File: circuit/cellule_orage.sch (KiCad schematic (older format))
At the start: 61 parts, among them Q1 BSS138, Q2 BSS138, Q3 BSS138, U2 TLC274, U4 LM555N, U5 TLP291

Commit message: V0.0 - Ready to route!
V0.0 - First release to routing, next step -> define all footprints
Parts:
- removed R4: 1M, symbol POT-RESCUE-cellule_orage
- removed R9: 50k, symbol POT-RESCUE-cellule_orage
- added D4: LBI_RED 2[mA], symbol Led_Small
- added Q4: MMBF170, SOT-23, symbol MMBF170
- added Q5: BSS138, SOT-23, symbol BSS138
- added R21: 114k, symbol R_Small
- added R22: 100k, symbol R_Small
- added R23: 140k, symbol R_Small
- added R26: 174, symbol R_Small
- added R4: 1M, symbol POT
- added R9: 50k, symbol POT
- added SW1: SPST, symbol SPST
- added U3: LM2903small, symbol LM2903small
- gave numbers to parts that had none: 24
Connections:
- net labels added: amplificator, captors, comparator, high-pass_filter, low-pass_filter, user_threshold
- net labels removed: Timer_out
- wire segments 179 -> 233
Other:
- note added: "Battery protection"
- note added: "Low battery display"
- note added: "User ON/OFF"
- note removed: "Circuit enable"
- moved on the sheet: C10, C12, C6, C7, C8, D1, L1, P5, P6, R14, R15, R24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

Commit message: Some schematic cleanup
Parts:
- C1, C10, C11, C12, C13, C2, C3, C4, C5, C7, C9: footprint (none) -> Capacitors_Tantalum_SMD:TantalC_SizeA_EIA-3216_Reflow
- C6, C8: footprint (none) -> Capacitors_SMD:c_elec_6.3x7.7
- D1: footprint (none) -> Diodes_ThroughHole:Diode_DO-41_SOD81_Horizontal_RM10
- D2, D3, D4: footprint (none) -> LEDs:LED-5MM
- L1: footprint (none) -> Choke_SMD:Choke_SMD_Wuerth-WE-PD2-Typ-L
- P1: footprint (none) -> Connect:USB_Micro-B
- P10, P7, P8: footprint (none) -> Socket_Strips:Socket_Strip_Straight_1x03
- P11: footprint (none) -> Socket_Strips:Socket_Strip_Straight_1x07
- P2, P3, P4: footprint (none) -> Socket_Strips:Socket_Strip_Angled_1x02
- Q1, Q2, Q3, Q4, Q5: footprint SOT-23 -> TO_SOT_Packages_SMD:SOT-23
- R1, R10, R11, R12, R13, R14, R15, R16, R17, R18, R19, R2, R20, R21, R22, R23, R24, R25, R26, R3, R5, R6, R7, R8: footprint (none) -> Resistors_SMD:R_1206
- R9: footprint (none) -> Potentiometers:Potentiometer_WirePads_Small
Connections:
- wire segments 233 -> 198
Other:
- moved on the sheet: P3, P4, R10, R8

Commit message: Change location
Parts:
- P1: footprint Connect:USB_Micro-B -> (none)
- R4, R9: symbol POT -> POT-RESCUE-cellule_orage

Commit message: Added simulation file
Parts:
- added unit 2 of U3
- P1: footprint (none) -> Connectors:USB_Micro-B
- P2, P3, P4: footprint Socket_Strips:Socket_Strip_Angled_1x02 -> Socket_Strips:Socket_Strip_Straight_1x02
- U3, U4: footprint (none) -> SMD_Packages:SOIC-8-N
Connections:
- net +6V: now also U3.8 (V+)
- net GND: now also U3.4 (V-)
- no-connect marks 0 -> 1
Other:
- moved on the sheet: P11
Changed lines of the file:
@@
 F 0 "U4" H 8400 2250 50  0000 L CNN
 F 1 "LM555N" H 8400 1550 50  0000 L CNN
-F 2 "" H 8800 1900 50  0001 C CNN
+F 2 "SMD_Packages:SOIC-8-N" H 8800 1900 50  0001 C CNN
 F 3 "" H 8800 1900 50  0000 C CNN
 	1    8800 1900
@@
 $EndComp
 $Comp
-L GND #PWR42
+L GND #PWR43
 U 1 1 5774DA83
 P 11350 2050
-F 0 "#PWR42" H 11350 1800 50  0001 C CNN
+F 0 "#PWR43" H 11350 1800 50  0001 C CNN
 F 1 "GND" H 11350 1900 50  0000 C CNN
 F 2 "" H 11350 2050 50  0000 C CNN
@@
 Shutter - Focus - GND\nTip - Ring - Sleeve\nValid for Nikon/Canon
 $Comp
-L GND #PWR43
+L GND #PWR44
 U 1 1 577521FF
 P 11350 4100
-F 0 "#PWR43" H 11350 3850 50  0001 C CNN
+F 0 "#PWR44" H 11350 3850 50  0001 C CNN
 F 1 "GND" H 11350 3950 50  0000 C CNN
 F 2 "" H 11350 4100 50  0000 C CNN
@@
 timer_out
 $Comp
-L GND #PWR50
+L GND #PWR53
 U 1 1 57782279
 P 13100 4050
-F 0 "#PWR50" H 13100 3800 50  0001 C CNN
+F 0 "#PWR53" H 13100 3800 50  0001 C CNN
 F 1 "GND" H 13100 3900 50  0000 C CNN
 F 2 "" H 13100 4050 50  0000 C CNN
@@
 +3V
 $Comp
-L +6V #PWR48
+L +6V #PWR51
 U 1 1 57783492
 P 13000 2550
-F 0 "#PWR48" H 13000 2400 50  0001 C CNN
+F 0 "#PWR51" H 13000 2400 50  0001 C CNN
 F 1 "+6V" H 13000 2690 50  0000 C CNN
 F 2 "" H 13000 2550 50  0000 C CNN
@@
 $EndComp
 $Comp
-L GND #PWR45
+L GND #PWR48
 U 1 1 57887382
 P 11650 8300
-F 0 "#PWR45" H 11650 8050 50  0001 C CNN
+F 0 "#PWR48" H 11650 8050 50  0001 C CNN
 F 1 "GND" H 11650 8150 50  0000 C CNN
 F 2 "" H 11650 8300 50  0000 C CNN
@@
 $EndComp
 $Comp
-L GND #PWR46
+L GND #PWR49
 U 1 1 5788741D
 P 12300 8300
-F 0 "#PWR46" H 12300 8050 50  0001 C CNN
+F 0 "#PWR49" H 12300 8050 50  0001 C CNN
 F 1 "GND" H 12300 8150 50  0000 C CNN
 F 2 "" H 12300 8300 50  0000 C CNN
@@
 $EndComp
 $Comp
-L GND #PWR47
+L GND #PWR50
 U 1 1 578874B8
 P 12900 8300
-F 0 "#PWR47" H 12900 8050 50  0001 C CNN
+F 0 "#PWR50" H 12900 8050 50  0001 C CNN
 F 1 "GND" H 12900 8150 50  0000 C CNN
 F 2 "" H 12900 8300 50  0000 C CNN
@@
 $EndComp
 $Comp
-L +6V #PWR44
+L +6V #PWR47
 U 1 1 578875F7
 P 11650 7750
-F 0 "#PWR44" H 11650 7600 50  0001 C CNN
+F 0 "#PWR47" H 11650 7600 50  0001 C CNN
 F 1 "+6V" H 11650 7890 50  0000 C CNN
 F 2 "" H 11650 7750 50  0000 C CNN
@@
 $EndComp
 $Comp
-L GND #PWR49
+L GND #PWR52
 U 1 1 57ACA7FC
 P 13000 2850
-F 0 "#PWR49" H 13000 2600 50  0001 C CNN
+F 0 "#PWR52" H 13000 2600 50  0001 C CNN
 F 1 "GND" H 13000 2700 50  0000 C CNN
 F 2 "" H 13000 2850 50  0000 C CNN
@@
 F 0 "P2" H 1200 1800 50  0000 C CNN
 F 1 "Phototransistor BPW85" H 1200 2000 50  0000 C CNN
-F 2 "Socket_Strips:Socket_Strip_Angled_1x02" H 1200 1650 50  0001 C CNN
+F 2 "Socket_Strips:Socket_Strip_Straight_1x02" H 1200 1650 50  0001 C CNN
 F 3 "" H 1200 1650 50  0000 C CNN
 	1    1200 1650
@@
 Wire Wire Line
 	6250 2900 6250 2850
-Text GLabel 14850 3300 2    60   Input ~ 0
+Text GLabel 14700 4700 2    60   Input ~ 0
 timer_out
 Text GLabel 13250 2700 2    60   Input ~ 0
 buzzer_out
 Connection ~ 13100 2700
-Text GLabel 14850 3450 2    60   Input ~ 0
+Text GLabel 14700 4850 2    60   Input ~ 0
 led_out
-Text GLabel 14850 3600 2    60   Input ~ 0
+Text GLabel 14700 5000 2    60   Input ~ 0
 buzzer_out
 Text GLabel 12350 1050 1    60   Input ~ 0
 trig_out
-Text GLabel 14850 3750 2    60   Input ~ 0
+Text GLabel 14700 5150 2    60   Input ~ 0
 trig_out
 $Comp
-L GND #PWR52
+L GND #PWR55
 U 1 1 57CF8D34
-P 14850 3900
-F 0 "#PWR52" H 14850 3650 50  0001 C CNN
-F 1 "GND" H 14850 3750 50  0000 C CNN
-F 2 "" H 14850 3900 50  0000 C CNN
-F 3 "" H 14850 3900 50  0000 C CNN
-	1    14850 3900
+P 14700 5300
+F 0 "#PWR55" H 14700 5050 50  0001 C CNN
+F 1 "GND" H 14700 5150 50  0000 C CNN
+F 2 "" H 14700 5300 50  0000 C CNN
+F 3 "" H 14700 5300 50  0000 C CNN
+	1    14700 5300
 	1    0    0    -1
 $EndComp
@@
 L CONN_01X07 P11
 U 1 1 57CF9A01
-P 14400 3450
-F 0 "P11" H 14400 3850 50  0000 C CNN
-F 1 "OUTPUT" V 14500 3450 50  0000 C CNN
-F 2 "Socket_Strips:Socket_Strip_Straight_1x07" H 14400 3450 50  0001 C CNN
-F 3 "" H 14400 3450 50  0000 C CNN
-	1    14400 3450
-	-1   0    0    1
-$EndComp
-Text GLabel 14850 3150 2    60   Input ~ 0
+P 14250 4850
+F 0 "P11" H 14250 5250 50  0000 C CNN
+F 1 "OUTPUT" V 14350 4850 50  0000 C CNN
+F 2 "Socket_Strips:Socket_Strip_Straight_1x07" H 14250 4850 50  0001 C CNN
+F 3 "" H 14250 4850 50  0000 C CNN
+	1    14250 4850
+	-1   0    0    1
+$EndComp
+Text GLabel 14700 4550 2    60   Input ~ 0
 +3V
 $Comp
-L +6V #PWR51
+L +6V #PWR54
 U 1 1 57CFE16A
-P 14850 3000
-F 0 "#PWR51" H 14850 2850 50  0001 C CNN
-F 1 "+6V" H 14850 3140 50  0000 C CNN
-F 2 "" H 14850 3000 50  0000 C CNN
-F 3 "" H 14850 3000 50  0000 C CNN
-	1    14850 3000
-	1    0    0    -1
-$EndComp
-Wire Wire Line
-	14600 3450 14850 3450
-Wire Wire Line
-	14600 3350 14800 3350
-Wire Wire Line
-	14800 3350 14800 3300
-Wire Wire Line
-	14800 3300 14850 3300
-Wire Wire Line
-	14600 3250 14750 3250
-Wire Wire Line
-	14750 3250 14750 3150
-Wire Wire Line
-	14750 3150 14850 3150
-Wire Wire Line
-	14600 3150 14700 3150
-Wire Wire Line
-	14700 3150 14700 3000
-Wire Wire Line
-	14700 3000 14850 3000
-Wire Wire Line
-	14600 3550 14800 3550
-Wire Wire Line
-	14800 3550 14800 3600
-Wire Wire Line
-	14800 3600 14850 3600
-Wire Wire Line
-	14600 3650 14750 3650
-Wire Wire Line
-	14750 3650 14750 3750
-Wire Wire Line
-	14750 3750 14850 3750
-Wire Wire Line
-	14600 3750 14700 3750
-Wire Wire Line
-	14700 3750 14700 3900
-Wire Wire Line
-	14700 3900 14850 3900
+P 14700 4400
+F 0 "#PWR54" H 14700 4250 50  0001 C CNN
+F 1 "+6V" H 14700 4540 50  0000 C CNN
+F 2 "" H 14700 4400 50  0000 C CNN
+F 3 "" H 14700 4400 50  0000 C CNN
+	1    14700 4400
+	1    0    0    -1
+$EndComp
+Wire Wire Line
+	14450 4850 14700 4850
+Wire Wire Line
+	14450 4750 14650 4750
+Wire Wire Line
+	14650 4750 14650 4700
+Wire Wire Line
+	14650 4700 14700 4700
+Wire Wire Line
+	14450 4650 14600 4650
+Wire Wire Line
+	14600 4650 14600 4550
+Wire Wire Line
+	14600 4550 14700 4550
+Wire Wire Line
+	14450 4550 14550 4550
+Wire Wire Line
+	14550 4550 14550 4400
+Wire Wire Line
+	14550 4400 14700 4400
+Wire Wire Line
+	14450 4950 14650 4950
+Wire Wire Line
+	14650 4950 14650 5000
+Wire Wire Line
+	14650 5000 14700 5000
+Wire Wire Line
+	14450 5050 14600 5050
+Wire Wire Line
+	14600 5050 14600 5150
+Wire Wire Line
+	14600 5150 14700 5150
+Wire Wire Line
+	14450 5150 14550 5150
+Wire Wire Line
+	14550 5150 14550 5300
+Wire Wire Line
+	14550 5300 14700 5300
 $Comp
 L CONN_01X02 P3
@@
 F 0 "P3" H 1200 2450 50  0000 C CNN
 F 1 "Phototransistor BPW85" H 1200 2650 50  0000 C CNN
-F 2 "Socket_Strips:Socket_Strip_Angled_1x02" H 1200 2300 50  0001 C CNN
+F 2 "Socket_Strips:Socket_Strip_Straight_1x02" H 1200 2300 50  0001 C CNN
 F 3 "" H 1200 2300 50  0000 C CNN
 	1    1200 2300
@@
 F 0 "P4" H 1200 3100 50  0000 C CNN
 F 1 "Phototransistor BPW85" H 1200 3300 50  0000 C CNN
-F 2 "Socket_Strips:Socket_Strip_Angled_1x02" H 1200 2950 50  0001 C CNN
+F 2 "Socket_Strips:Socket_Strip_Straight_1x02" H 1200 2950 50  0001 C CNN
 F 3 "" H 1200 2950 50  0000 C CNN
 	1    1200 2950
@@
 Text Notes 10450 7650 0    60   ~ 0
 Max 500 [mA]
-Text Notes 15000 2900 0    60   ~ 0
+Text Notes 14850 4300 0    60   ~ 0
 Max 500 [mA]
-Text Notes 15150 3200 0    60   ~ 0
+Text Notes 15000 4600 0    60   ~ 0
 Max 150 [mA]
 $Comp
@@
 F 0 "U3" H 6200 9350 50  0000 C CNN
 F 1 "LM2903small" H 6150 9150 50  0000 L CNN
-F 2 "" H 6100 9250 50  0001 C CNN
+F 2 "SMD_Packages:SOIC-8-N" H 6100 9250 50  0001 C CNN
 F 3 "" H 6100 9250 50  0000 C CNN
 	1    6100 9250
@@
 	6350 3150 7000 3150
 $Sheet
-S 3500 6000 650  350
+S 2700 5550 650  350
 U 584818FE
 F0 "power" 60
 F1 "power.sch" 60
-F2 "+6v" O R 4150 6100 60
-F3 "+3V" O R 4150 6200 60
-F4 "GND" O R 4150 6300 60
+F2 "+6v" O R 3350 5650 60
+F3 "+3V" O R 3350 5750 60
+F4 "GND" O R 3350 5850 60
 $EndSheet
 $Comp
@@
 F 0 "P1" H 1125 7625 50  0000 C CNN
 F 1 "USB_OTG" H 800 7950 50  0000 C CNN
-F 2 "" V 750 7650 50  0000 C CNN
+F 2 "Connectors:USB_Micro-B" V 750 7650 50  0001 C CNN
 F 3 "" V 750 7650 50  0000 C CNN
 	1    800  7750
 	0    -1   1    0
 $EndComp
+$Comp
+L LM2903small U3
+U 2 1 58766CE8
+P 8600 3050
+F 0 "U3" H 8700 3150 50  0000 C CNN
+F 1 "LM2903small" H 8650 2950 50  0000 L CNN
+F 2 "SMD_Packages:SOIC-8-N" H 8600 3050 50  0001 C CNN
+F 3 "" H 8600 3050 50  0000 C CNN
+	2    8600 3050
+	1    0    0    -1
+$EndComp
+$Comp
+L GND #PWR46
+U 1 1 58766E18
+P 8600 3250
+F 0 "#PWR46" H 8600 3000 50  0001 C CNN
+F 1 "GND" H 8600 3100 50  0000 C CNN
+F 2 "" H 8600 3250 50  0000 C CNN
+F 3 "" H 8600 3250 50  0000 C CNN
+	1    8600 3250
+	1    0    0    -1
+$EndComp
+$Comp
+L +6V #PWR45
+U 1 1 58766F13
+P 8600 2850
+F 0 "#PWR45" H 8600 2700 50  0001 C CNN
+F 1 "+6V" H 8600 2990 50  0000 C CNN
+F 2 "" H 8600 2850 50  0000 C CNN
+F 3 "" H 8600 2850 50  0000 C CNN
+	1    8600 2850
+	1    0    0    -1
+$EndComp
+Wire Wire Line
+	8600 2900 8600 2850
+Wire Wire Line
+	8600 3250 8600 3200
+NoConn ~ 8850 3050
 $EndSCHEMATC

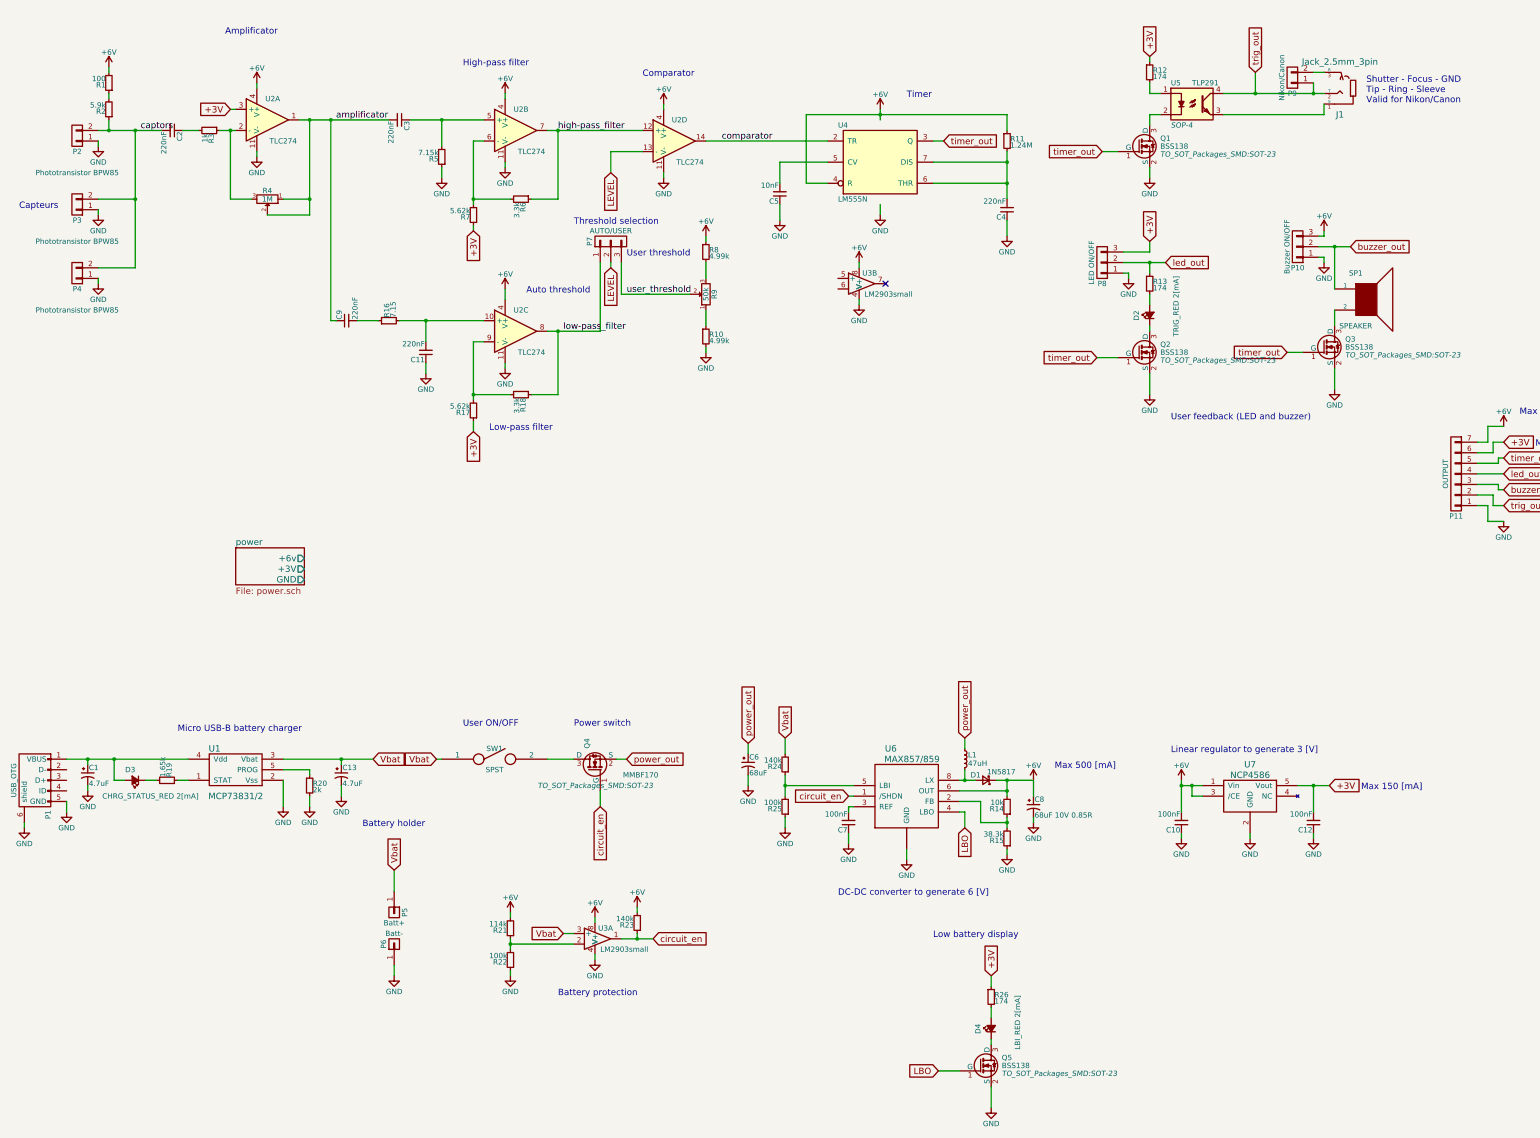
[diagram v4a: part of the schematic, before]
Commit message: Update schematic and simulations
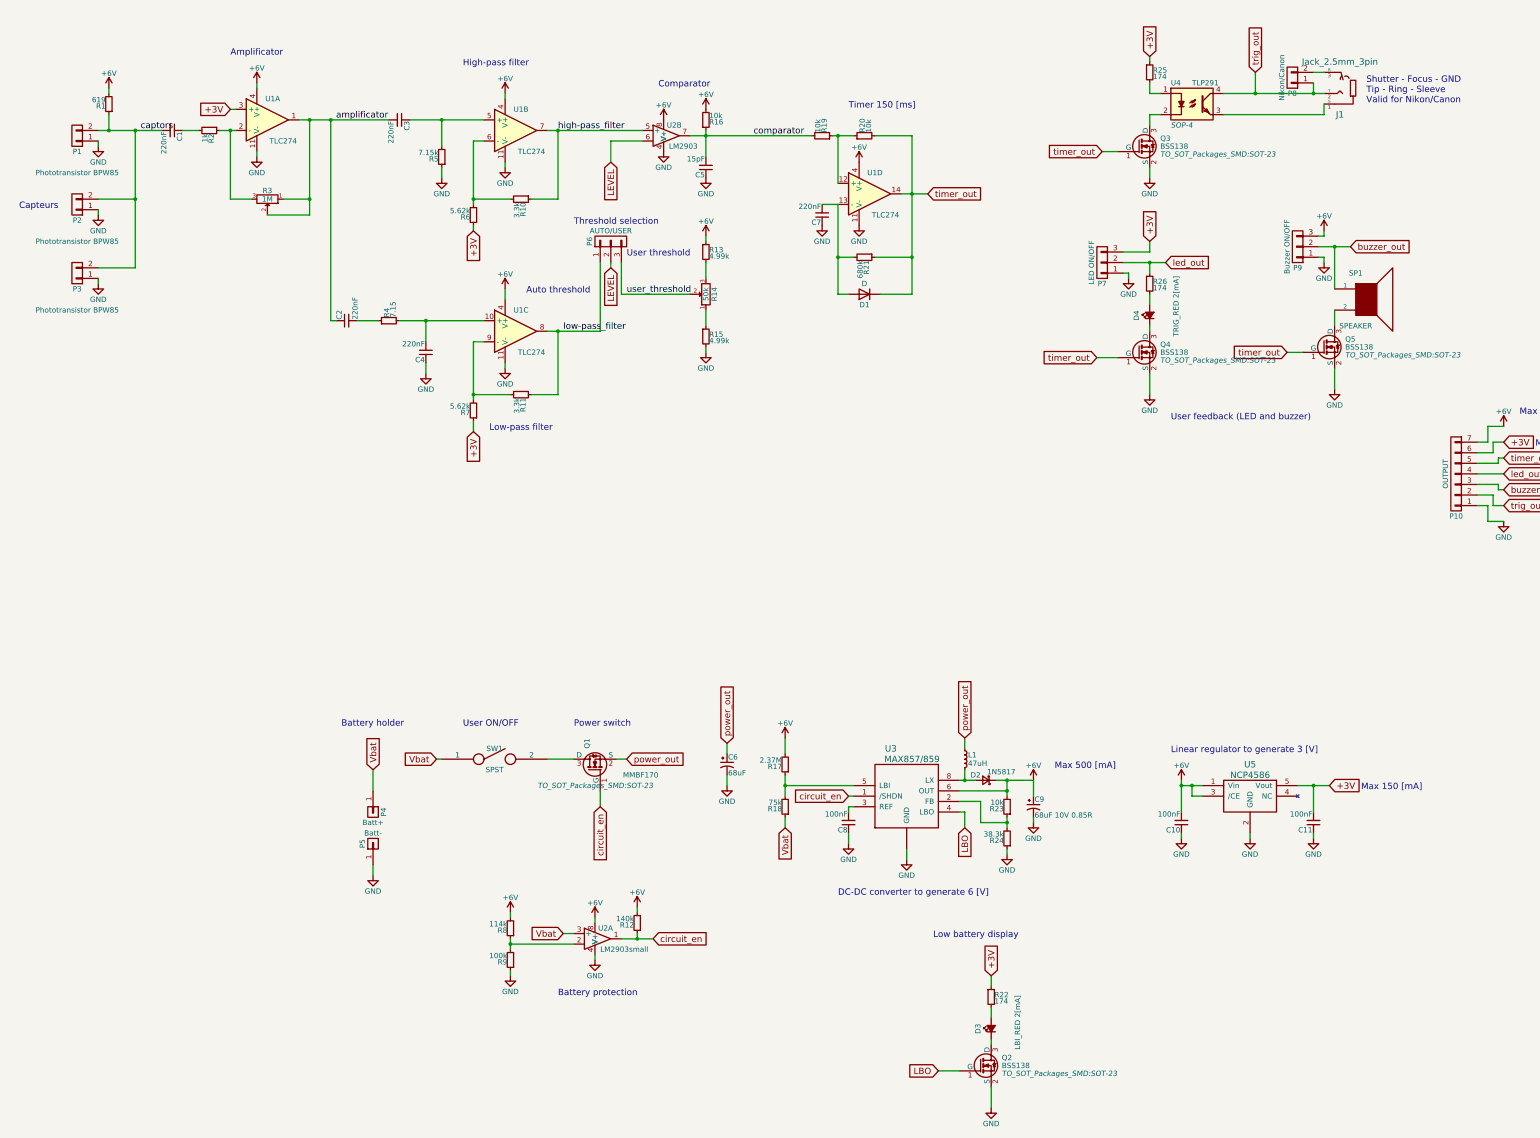
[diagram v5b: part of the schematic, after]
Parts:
- removed C1, C13: 4.7uF, Capacitors_Tantalum_SMD:TantalC_SizeA_EIA-3216_Reflow, symbol CP1_Small
- removed C4: 220nF, Capacitors_Tantalum_SMD:TantalC_SizeA_EIA-3216_Reflow, symbol C_Small
- removed D3: CHRG_STATUS_RED 2[mA], LEDs:LED-5MM, symbol Led_Small
- removed P1: USB_OTG, Connectors:USB_Micro-B, symbol USB_OTG
- removed R11: 1.24M, Resistors_SMD:R_1206, symbol R_Small
- removed R2: 5.9k, Resistors_SMD:R_1206, symbol R_Small
- removed U1: MCP73831/2, symbol MCP73831/2
- removed U4: LM555N, SMD_Packages:SOIC-8-N, symbol LM555N
- added C7: 220nF, Capacitors_Tantalum_SMD:TantalC_SizeA_EIA-3216_Reflow, symbol C_Small
- added D1: D, symbol D
- added R16: 10k, Resistors_SMD:R_1206, symbol R_Small
- added R21: 680k, Resistors_SMD:R_1206, symbol R_Small
- C5: value 10nF -> 15pF
- R1: value 100 -> 619
- R17: renamed from R24; value 140k -> 2.37M
- R18: renamed from R25; value 100k -> 75k
- R19: value 1.65k -> 10k
- R20: value 2k -> 10k
- U2: renamed from U3; value LM2903small -> LM2903
- renumbered C2 to C1, C12 to C11, C9 to C2, C11 to C4, C7 to C8, C8 to C9, D1 to D2, D4 to D3, D2 to D4, P2 to P1, P11 to P10, P3 to P2, P4 to P3, P5 to P4, P6 to P5, P7 to P6, P8 to P7, P9 to P8, P10 to P9, Q4 to Q1, Q5 to Q2, Q1 to Q3, Q2 to Q4, Q3 to Q5, R6 to R10, R18 to R11, R23 to R12, R8 to R13, R9 to R14, R10 to R15, R3 to R2, R26 to R22, R14 to R23, R15 to R24, R12 to R25, R13 to R26, R4 to R3, R16 to R4, R7 to R6, R17 to R7, R21 to R8, R22 to R9, U2 to U1, U3 to U2, U6 to U3, U5 to U4, U7 to U5
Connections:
- net +6V: now also R17.2, R16.2
- net GND: now also C7.1; no longer R18.1, R20.2
- net LEVEL: now also U2.6 (_); no longer U1.13 (-)
- net Vbat: now also R18.1; no longer R17.2
- net captors: now also R1.1
- net comparator: now also C5.2, R19.2, U2.7, R16.1; no longer U1.14
- net high-pass_filter: now also U2.5 (+); no longer U1.12 (+)
- net timer_out: now also R20.2, U1.14, D1.1 (K), R21.1
- net at R19.1: now also R20.1, U1.12 (+)
- new net: C7.2, D1.2 (A), R21.2, U1.13 (-)
- no-connect marks 1 -> 0
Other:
- note added: "Timer 150 [ms]"
- note removed: "Micro USB-B battery charger"
- note removed: "Timer"
- moved on the sheet: C6, P4, P5, R1, U1D, U2B

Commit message: Commit before branch
Time to make a new branch for HES project!
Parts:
- removed J1: Jack_2.5mm_3pin, symbol Jack_3.5mm_3pin
- removed SP1: SPEAKER, symbol SPEAKER
- removed SW1: SPST, symbol SPST
- added LS1: Speaker, symbol Speaker
- added P11: Remote connection 1-R/2-T/3-S, Socket_Strips:Socket_Strip_Straight_1x03, symbol CONN_01X03
- added P12: User ON/OFF, Pin_Headers:Pin_Header_Straight_1x02_Pitch2.54mm, symbol CONN_01X02
- D1: value D -> 1N4148; footprint (none) -> Diodes_SMD:D_SOD-123
- P8: value Nikon/Canon -> Prefocus; footprint (none) -> Pin_Headers:Pin_Header_Straight_1x02_Pitch2.54mm
- U1: footprint (none) -> Housings_DIP:DIP-14_W7.62mm
- U2: value LM2903small -> LM2903
- U3: footprint (none) -> Housings_SOIC:SOIC-8_3.9x4.9mm_Pitch1.27mm
- U5: footprint (none) -> TO_SOT_Packages_SMD:SOT-23-5
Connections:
- net Vbat: now also P12.1 (P1)
- net buzzer_out: now also LS1.1
- net trig_out: now also P11.1 (P1)
- net at U4.3: now also P11.3 (P3)
- net at Q5.3 (D): now also LS1.2
- net at P8.2 (P2): now also P11.2 (P2)
- net at Q1.3 (D): now also P12.2 (P2)
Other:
- note added: "Ajouter découplages"
- note added: "Découpler ampli des filtres -> suiveur (attention nouveau boitier, trouver mieux)"
- note added: "Shutter - Focus - GND\nTip - Ring - Sleeve\nConnect 1-2 to prefocus\nValid for Nikon/Canon"
- note removed: "Shutter - Focus - GND\nTip - Ring - Sleeve\nValid for Nikon/Canon"
- moved on the sheet: P8
